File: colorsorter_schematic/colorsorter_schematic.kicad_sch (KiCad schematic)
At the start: 23 parts, among them SW2 SW_SPDT, U1 PIC24FJ64GA702-I/SO, U2 ESP8266-01_ESP-01

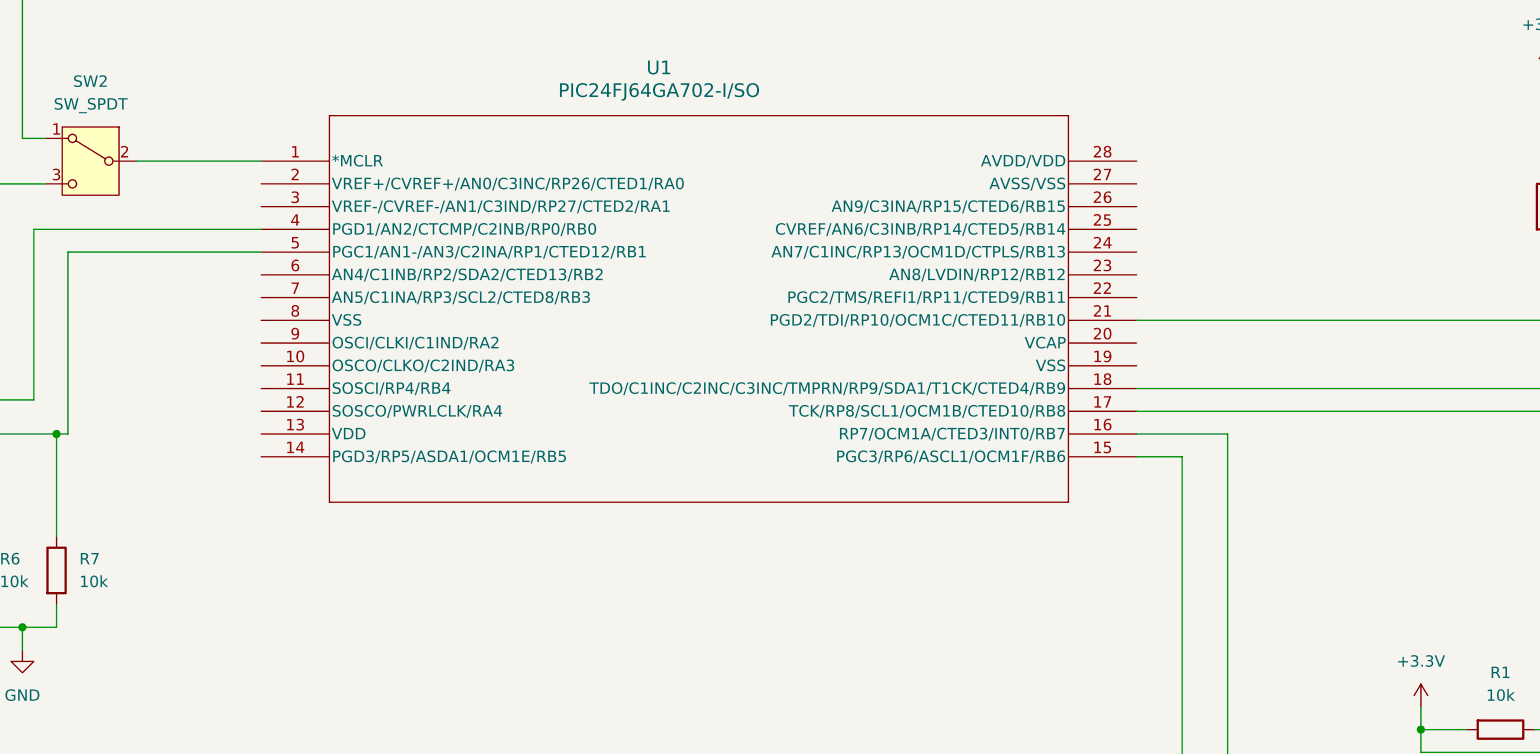
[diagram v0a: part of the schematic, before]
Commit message: Issue #10 : Projektovanje električne šeme - minimalni broj pinova
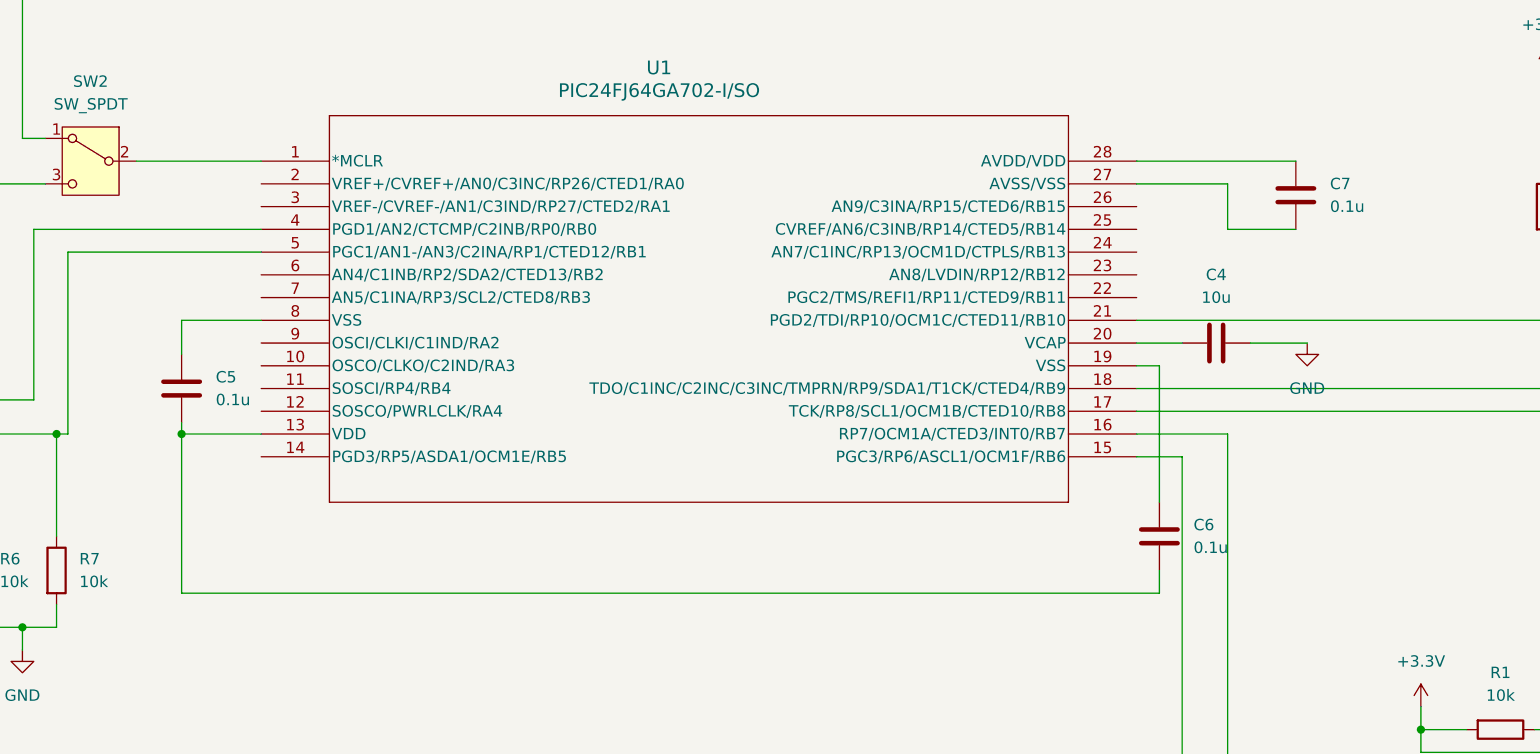
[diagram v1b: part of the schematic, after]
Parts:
- added C4: 10u, symbol Device:C
- added C5, C6, C7: 0.1u, symbol Device:C
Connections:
- net GND: now also C4.1
- net at U1.13 (VDD): now also C5.2, C6.2
- net at U1.19 (VSS): now also C6.1
- net at U1.20 (VCAP): now also C4.2
- net at U1.27 (AVSS/VSS): now also C7.2
- net at U1.28 (AVDD/VDD): now also C7.1
- net at U1.8 (VSS): now also C5.1

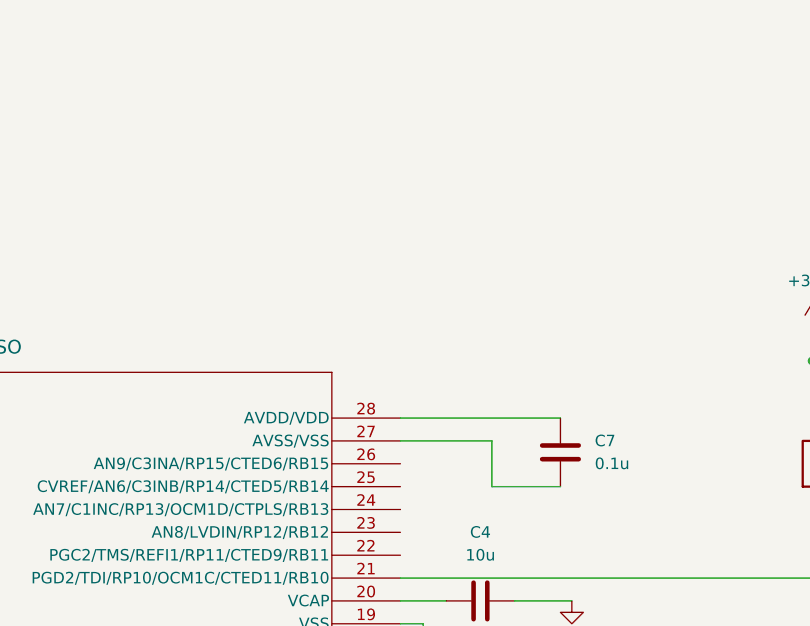
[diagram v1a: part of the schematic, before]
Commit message: Issue #14 : Projektovanje električne šeme - taster
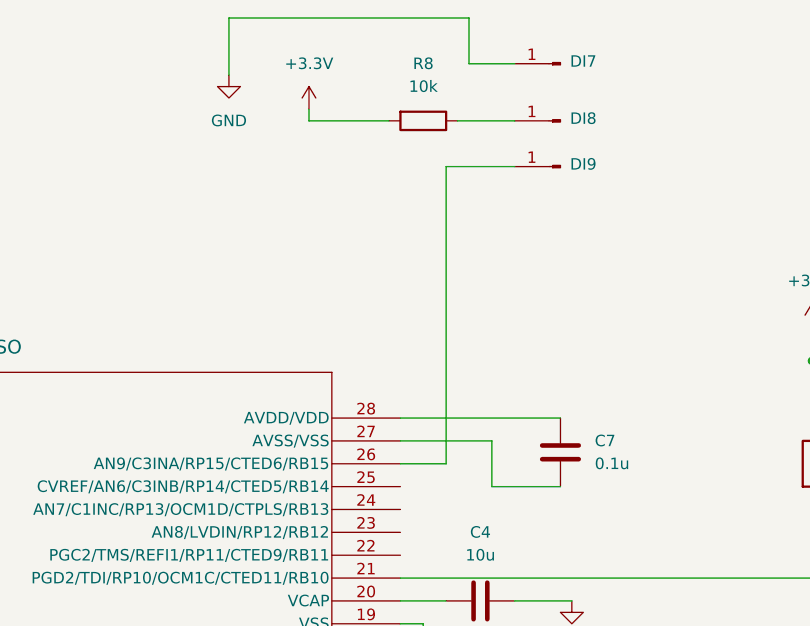
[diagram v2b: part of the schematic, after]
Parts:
- added DI7, DI8, DI9: Conn_01x01_Pin, symbol Connector:Conn_01x01_Pin
- added R8: 10k, Resistor_SMD:R_0805_2012Metric, symbol Device:R
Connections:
- net +3.3V: now also R8.2
- net GND: now also DI7.1 (Pin_1)
- net at U1.26 (AN9/C3INA/RP15/CTED6/RB15): now also DI9.1 (Pin_1)
- new net: DI8.1 (Pin_1), R8.1

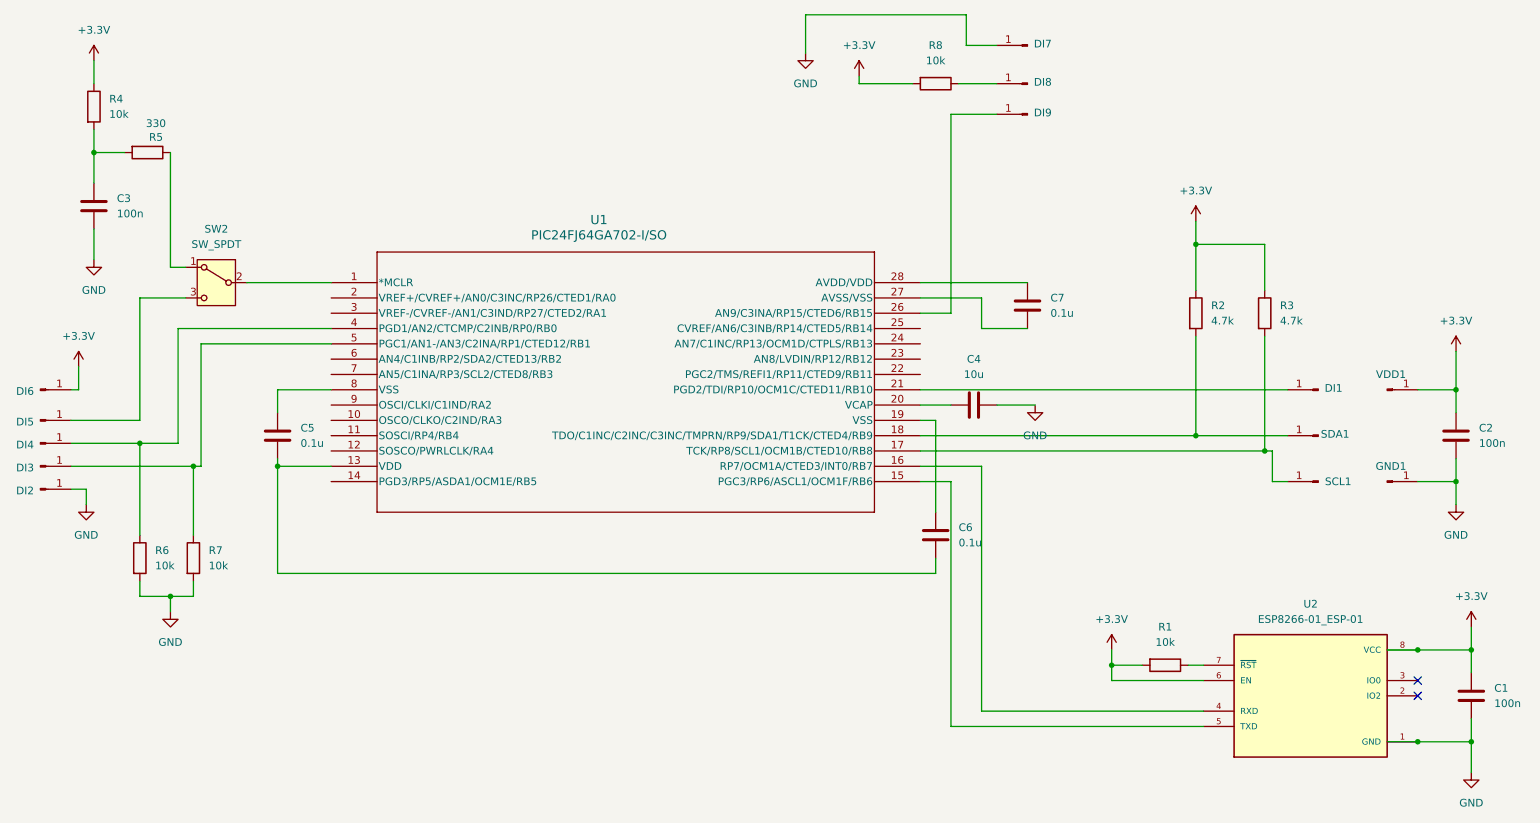
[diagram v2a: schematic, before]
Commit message: Issue #13 : Projektovanje električne šeme - servo motor
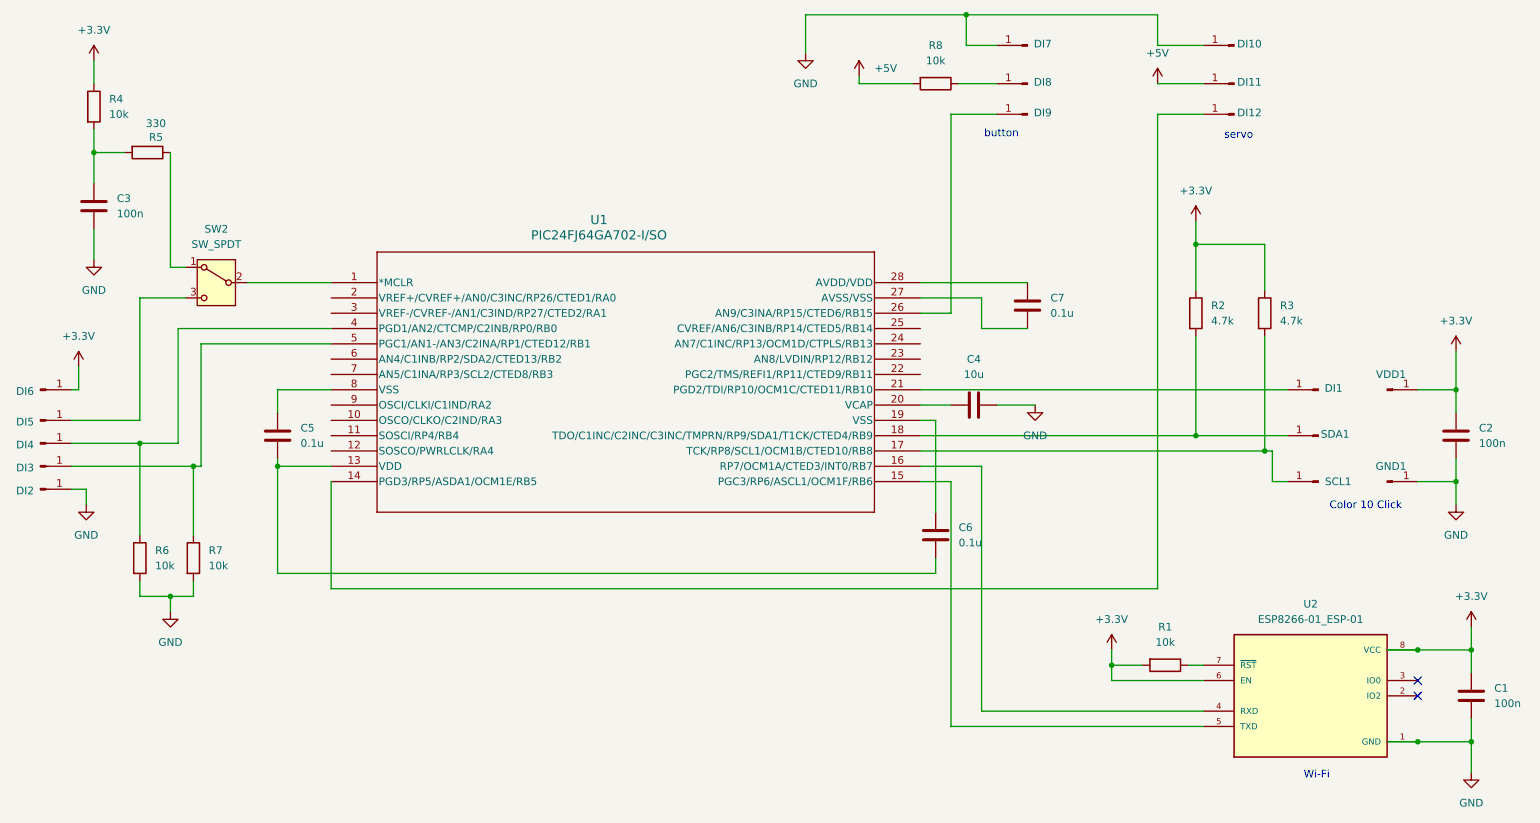
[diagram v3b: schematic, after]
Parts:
- added DI10, DI11, DI12: Conn_01x01_Pin, symbol Connector:Conn_01x01_Pin
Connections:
- net +3.3V: no longer R8.2
- net GND: now also DI10.1 (Pin_1)
- net at U1.14 (PGD3/RP5/ASDA1/OCM1E/RB5): now also DI12.1 (Pin_1)
- new net +5V: DI11.1 (Pin_1), R8.2
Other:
- note added: "Color 10 Click"
- note added: "Wi-Fi"
- note added: "button"
- note added: "servo"

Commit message: Issue #18:
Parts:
- added DI13, DI14, DI15: Conn_01x01_Pin, symbol Connector:Conn_01x01_Pin
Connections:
- net +5V: now also DI14.1 (Pin_1)
- net GND: now also DI13.1 (Pin_1)
- net at U1.25 (CVREF/AN6/C3INB/RP14/CTED5/RB14): now also DI15.1 (Pin_1)
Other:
- note added: "LED"

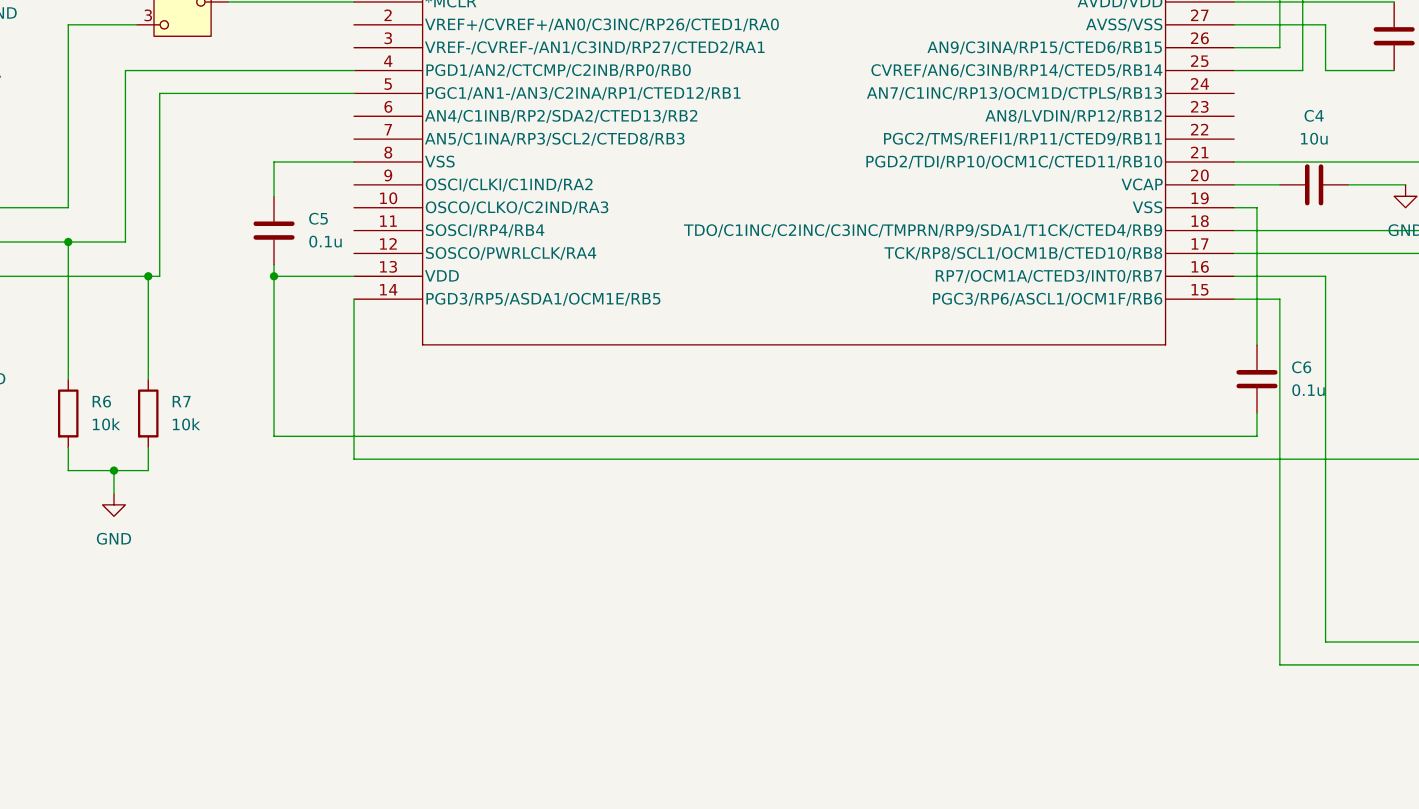
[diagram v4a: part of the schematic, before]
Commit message: Issue #15 : Konfiguracija oscilatora
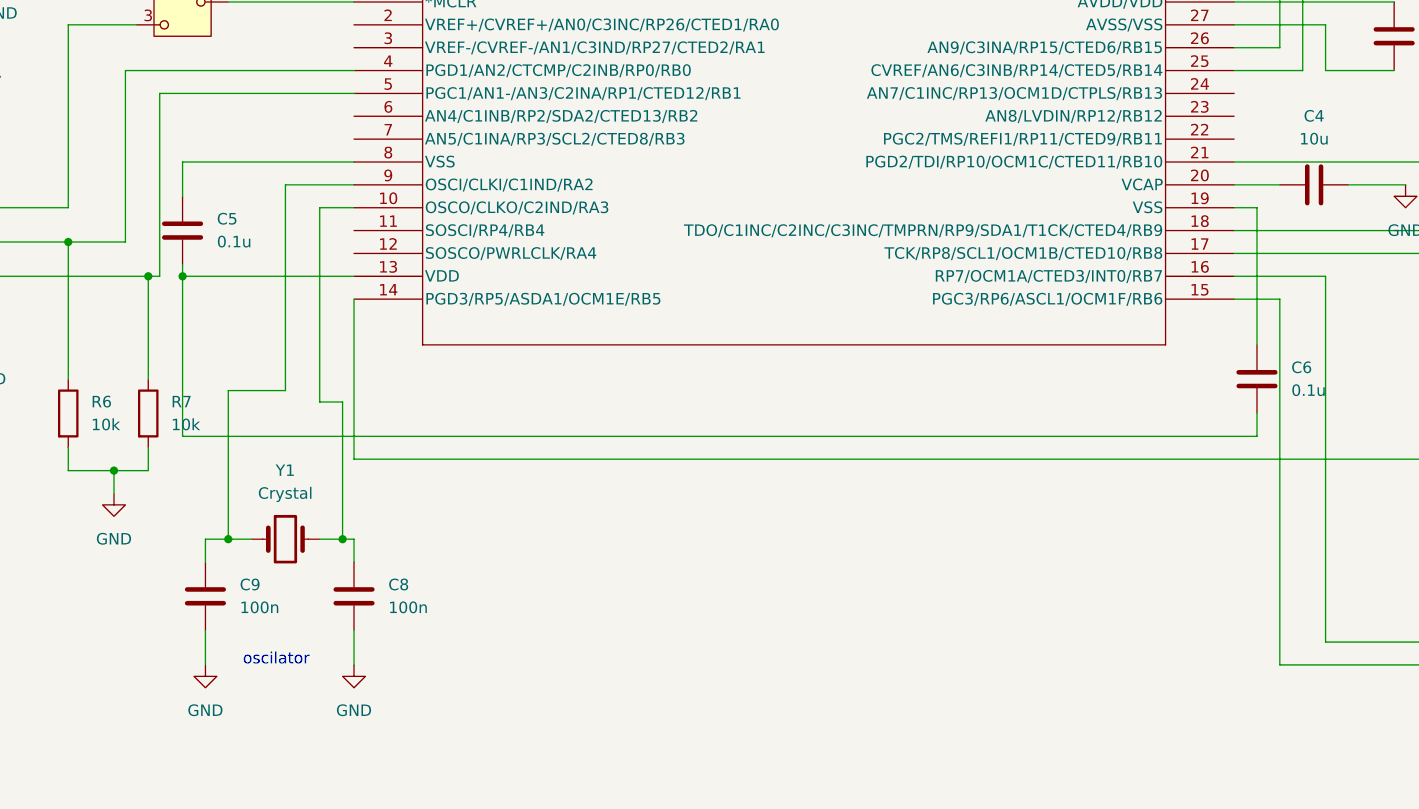
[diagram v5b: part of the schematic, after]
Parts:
- added C8, C9: 100n, symbol Device:C
- added Y1: Crystal, symbol Device:Crystal
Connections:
- net GND: now also C8.2, C9.2
- net at U1.10 (OSCO/CLKO/C2IND/RA3): now also C8.1, Y1.2
- net at U1.9 (OSCI/CLKI/C1IND/RA2): now also C9.1, Y1.1
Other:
- note added: "oscilator"
- moved on the sheet: C5
